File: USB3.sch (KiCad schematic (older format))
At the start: 0 parts

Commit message: Added USB SRAM sheet,Added USB3 ethernet ic
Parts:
- added C?: 100nF, Capacitor_SMD:C_0603_1608Metric_Pad1.08x0.95mm_HandSolder, symbol Device:C_Small
- added IC?: M24M02-DRMN6TP, SOIC127P600X175-8N, symbol GM_Memory_EEPROM:M24M02-DRMN6TP
- added R? (x2): 2K, Resistor_SMD:R_0603_1608Metric_Pad0.98x0.95mm_HandSolder, symbol Device:R_Small_US
- added U? (x3): CYUSB3014-BZXI, Package_BGA:BGA121C80P11X11_1000X1000X120, symbol GM_Microcontrollers:CYUSB3014-BZXI
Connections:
- net labels added: DQ[0:15], DQ[16:31], GNDD, I2C_SCL, I2C_SDA, V3P3
- wire segments 0 -> 49
- no-connect marks 0 -> 5

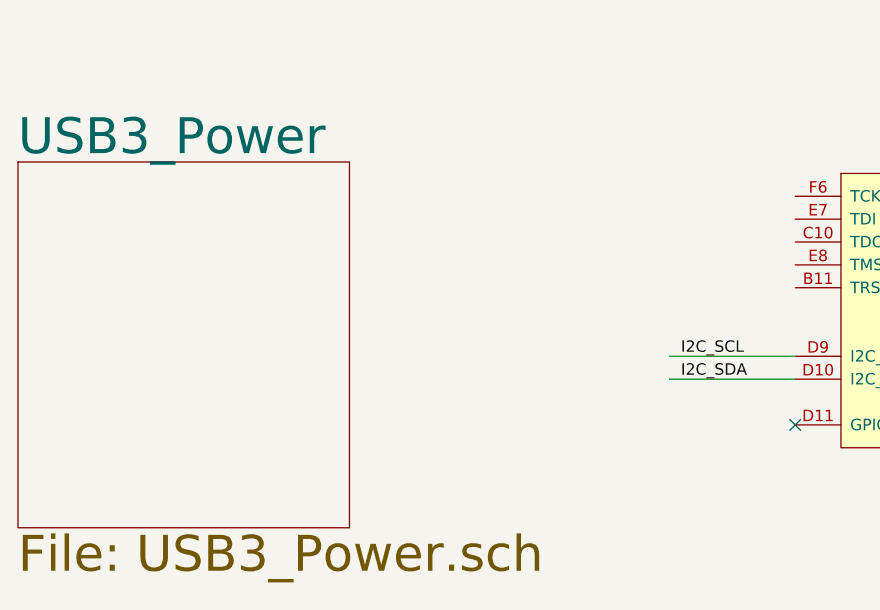
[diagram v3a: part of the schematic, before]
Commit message: Added USB3 SRAM Added 5V regulator
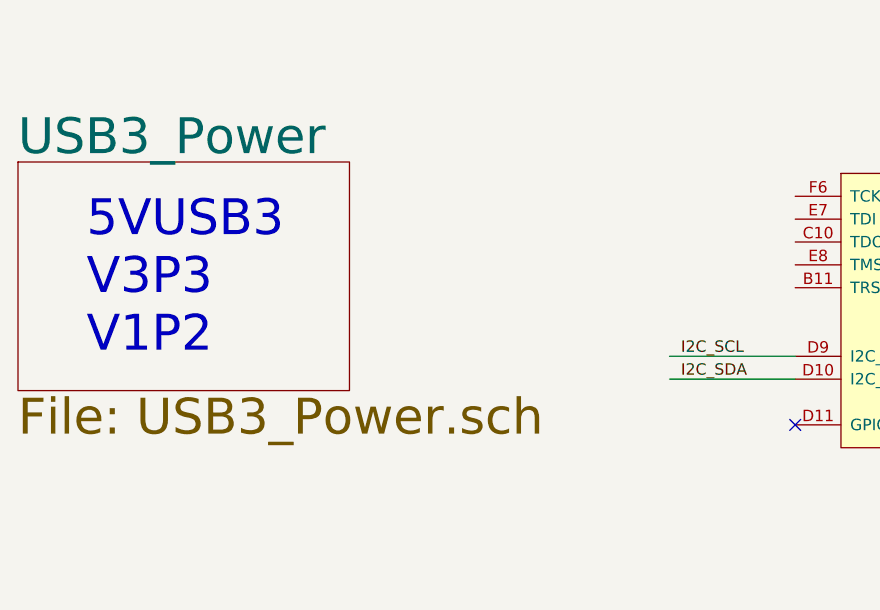
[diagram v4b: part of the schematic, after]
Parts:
- removed C?: 100nF, Capacitor_SMD:C_0603_1608Metric_Pad1.08x0.95mm_HandSolder, symbol Device:C_Small
- removed IC?: M24M02-DRMN6TP, SOIC127P600X175-8N, symbol GM_Memory_EEPROM:M24M02-DRMN6TP
- removed R?: 2K, Resistor_SMD:R_0603_1608Metric_Pad0.98x0.95mm_HandSolder, symbol Device:R_Small_US
- removed U? (x3): CYUSB3014-BZXI, Package_BGA:BGA121C80P11X11_1000X1000X120, symbol GM_Microcontrollers:CYUSB3014-BZXI
- added C?: 100nF, Capacitor_SMD:C_0603_1608Metric_Pad1.08x0.95mm_HandSolder, symbol Device:C_Small
- added IC?: M24M02-DRMN6TP, SOIC127P600X175-8N, symbol GM_Memory_EEPROM:M24M02-DRMN6TP
- added R?: 2K, Resistor_SMD:R_0603_1608Metric_Pad0.98x0.95mm_HandSolder, symbol Device:R_Small_US
- added U? (x3): CYUSB3014-BZXI, Package_BGA:BGA121C80P11X11_1000X1000X120, symbol GM_Microcontrollers:CYUSB3014-BZXI
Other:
- note added: "5VUSB3\nV3P3\nV1P2"
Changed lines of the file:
@@
 $EndDescr
 $Sheet
-S 750  5700 1450 1600
-U 60277424
+S 750  5700 1450 1000
+U 603E2782
 F0 "USB3_Power" 157
 F1 "USB3_Power.sch" 157
@@
 $Comp
 L GM_Microcontrollers:CYUSB3014-BZXI U?
-U 2 1 603A79A2
+U 2 1 603E3C7F
 P 4350 1250
 F 0 "U?" H 5000 1415 50  0000 C CNN
@@
 $Comp
 L GM_Microcontrollers:CYUSB3014-BZXI U?
-U 3 1 603A9E58
+U 3 1 603E3C80
 P 4350 5750
 F 0 "U?" H 5218 5196 50  0000 L CNN
@@
 $Comp
 L GM_Microcontrollers:CYUSB3014-BZXI U?
-U 4 1 603AE481
+U 4 1 603E2786
 P 6350 5750
 F 0 "U?" H 6928 5196 50  0000 L CNN
@@
 $Comp
 L GM_Memory_EEPROM:M24M02-DRMN6TP IC?
-U 1 1 603D536E
+U 1 1 603E2787
 P 9200 5600
 F 0 "IC?" H 9650 5765 50  0000 C CNN
@@
 $Comp
 L Device:C_Small C?
-U 1 1 603E2400
+U 1 1 603E2788
 P 8150 5800
-AR Path="/601DF0A6/603E2400" Ref="C?"  Part="1"
-AR Path="/601E7BBE/60277424/603E2400" Ref="C?"  Part="1"
-AR Path="/601E7BBE/603E2400" Ref="C?"  Part="1"
+AR Path="/601DF0A6/603E2788" Ref="C?"  Part="1"
+AR Path="/601E7BBE/60277424/603E2788" Ref="C?"  Part="1"
+AR Path="/601E7BBE/603E2788" Ref="C?"  Part="1"
 F 0 "C?" H 8242 5891 50  0000 L CNN
 F 1 "100nF" H 8242 5800 50  0000 L CNN
@@
 $Comp
 L power:GNDD #PWR?
-U 1 1 603E909D
+U 1 1 603E2789
 P 8150 5900
-AR Path="/601E7BBE/60277424/603E909D" Ref="#PWR?"  Part="1"
-AR Path="/601E7BBE/603E909D" Ref="#PWR?"  Part="1"
+AR Path="/601E7BBE/60277424/603E2789" Ref="#PWR?"  Part="1"
+AR Path="/601E7BBE/603E2789" Ref="#PWR?"  Part="1"
 F 0 "#PWR?" H 8150 5650 50  0001 C CNN
 F 1 "GNDD" H 8154 5745 50  0000 C CNN
@@
 $Comp
 L power:GNDD #PWR?
-U 1 1 603ED9AD
+U 1 1 603E278A
 P 10650 6000
-AR Path="/601E7BBE/60277424/603ED9AD" Ref="#PWR?"  Part="1"
-AR Path="/601E7BBE/603ED9AD" Ref="#PWR?"  Part="1"
+AR Path="/601E7BBE/60277424/603E278A" Ref="#PWR?"  Part="1"
+AR Path="/601E7BBE/603E278A" Ref="#PWR?"  Part="1"
 F 0 "#PWR?" H 10650 5750 50  0001 C CNN
 F 1 "GNDD" H 10654 5845 50  0000 C CNN
@@
 $Comp
 L Device:R_Small_US R?
-U 1 1 603F67A2
+U 1 1 603E278B
 P 8500 5900
 F 0 "R?" H 8568 5946 50  0000 L CNN
@@
 	8850 5700 8650 5700
 NoConn ~ 4150 6850
+Text Notes 1050 6550 0    157  ~ 0
+5VUSB3\nV3P3\nV1P2
 Wire Bus Line
 	3850 1200 3850 2950

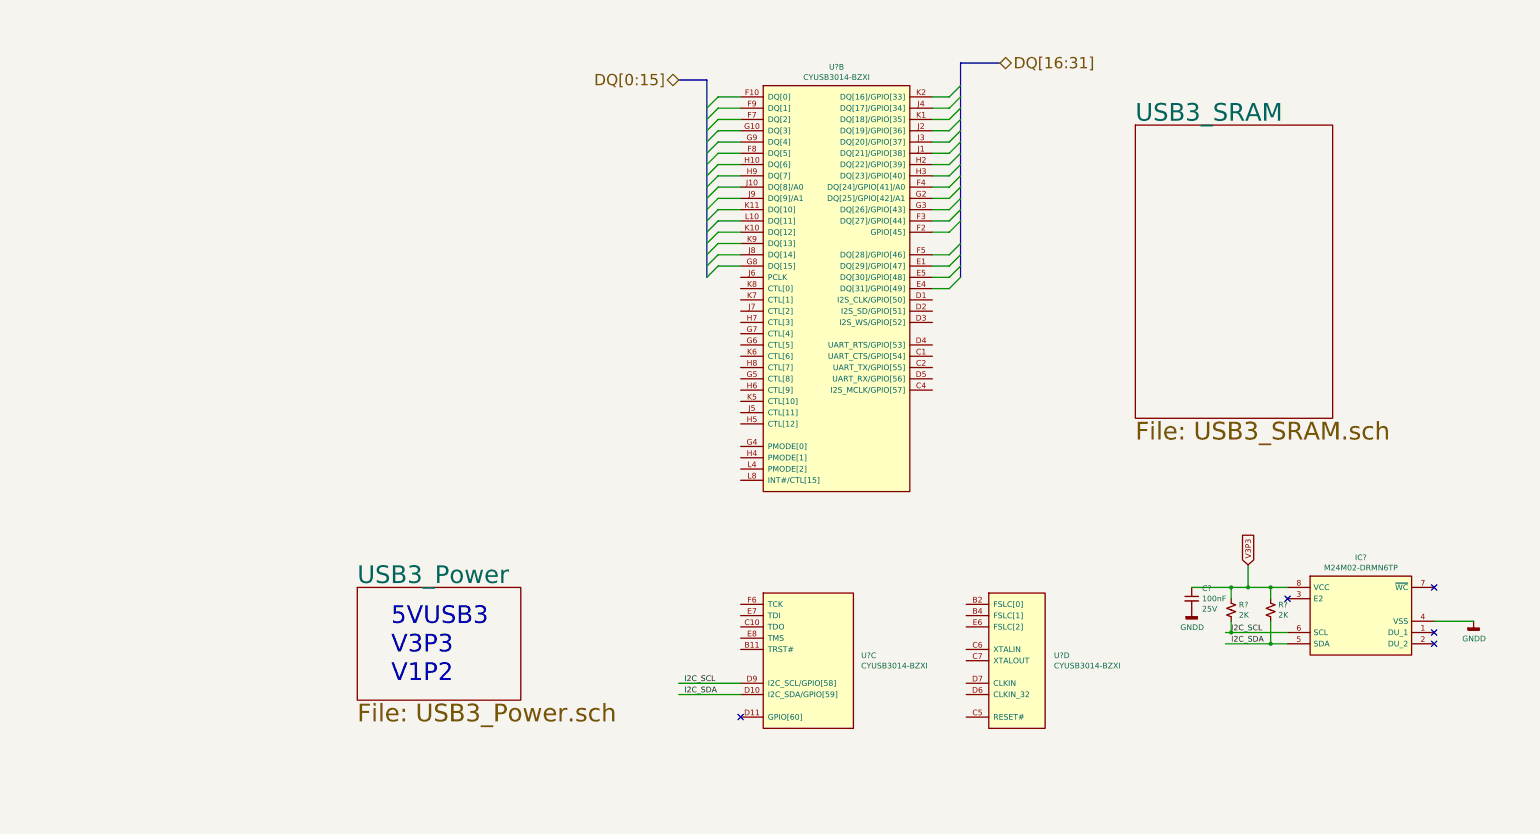
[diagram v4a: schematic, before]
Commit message: Added USB3 type B connector Added ESD protection to the same sheet
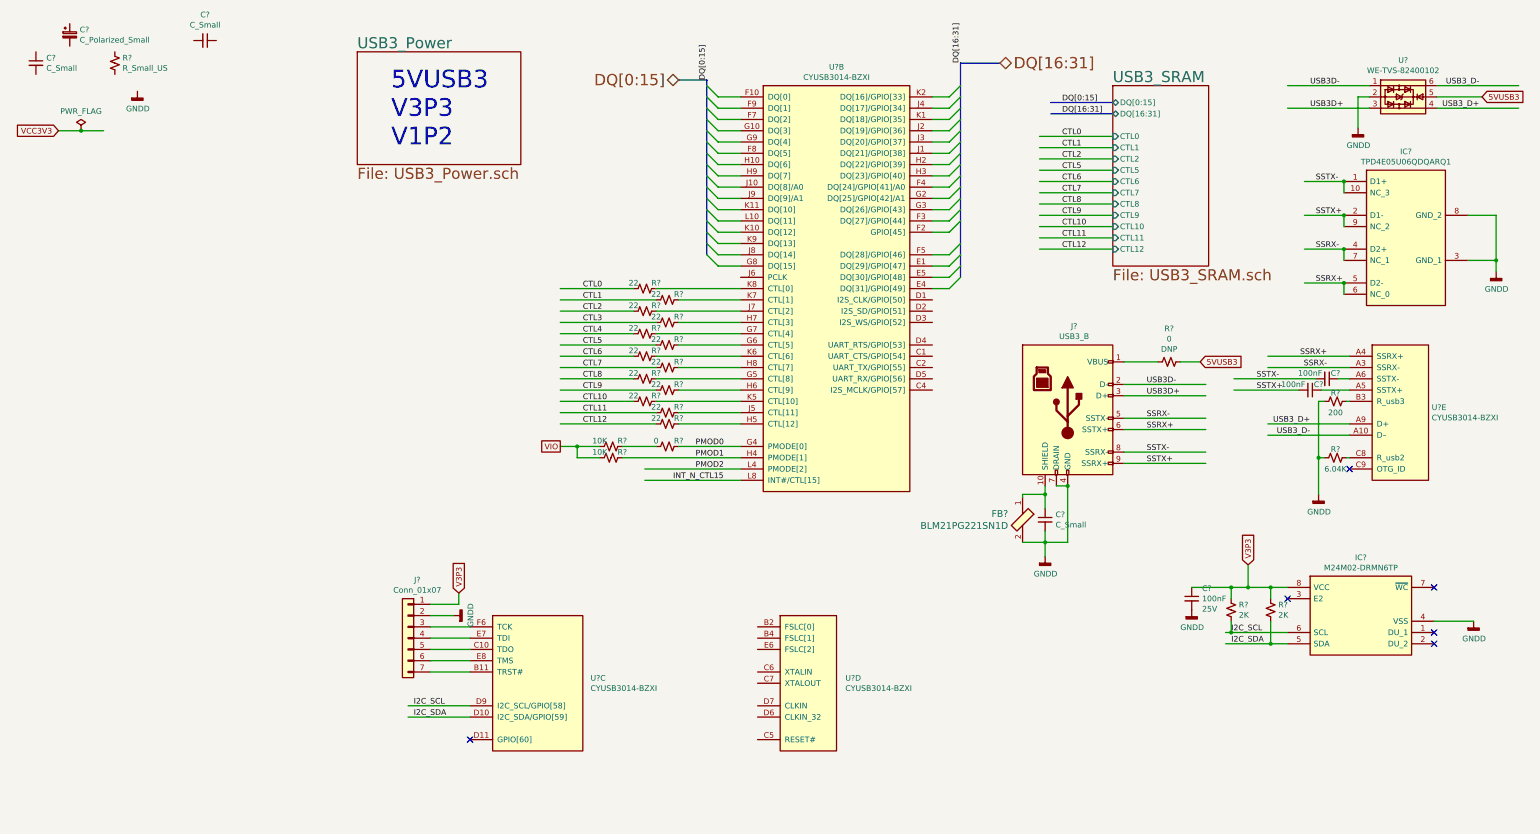
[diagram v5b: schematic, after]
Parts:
- added C? (x2): C_Small, Capacitor_SMD:C_0603_1608Metric_Pad1.08x0.95mm_HandSolder, symbol Device:C_Small
- added C?: C_Polarized_Small, Capacitor_Tantalum_SMD:CP_EIA-1608-10_AVX-L_Pad1.25x1.05mm_HandSolder, symbol Device:C_Polarized_Small
- added C?: C_Small, symbol Device:C_Small
- added C? (x2): 100nF, Capacitor_SMD:C_0402_1005Metric_Pad0.74x0.62mm_HandSolder, symbol Device:C_Small
- added FB?: BLM21PG221SN1D, digikey-footprints:0805, symbol dk_Ferrite-Beads-and-Chips:BLM21PG221SN1D
- added IC?: TPD4E05U06QDQARQ1, DQA(R-PUSON-N10), symbol GM_Protection:TPD4E05U06QDQARQ1
- added J?: Conn_01x07, symbol Connector_Generic:Conn_01x07
- added J?: USB3_B, GM_Connectors:GSB3211311WEU, symbol Connector:USB3_B
- added R?: R_Small_US, Resistor_SMD:R_0603_1608Metric_Pad0.98x0.95mm_HandSolder, symbol Device:R_Small_US
- added R? (x13): 22, Resistor_SMD:R_0603_1608Metric_Pad0.98x0.95mm_HandSolder, symbol Device:R_Small_US
- added R? (x2): 0, Resistor_SMD:R_0603_1608Metric_Pad0.98x0.95mm_HandSolder, symbol Device:R_Small_US
- added R? (x2): 10K, Resistor_SMD:R_0603_1608Metric_Pad0.98x0.95mm_HandSolder, symbol Device:R_Small_US
- added R?: 200, Resistor_SMD:R_0603_1608Metric_Pad0.98x0.95mm_HandSolder, symbol Device:R_Small_US
- added R?: 6.04K, Resistor_SMD:R_0603_1608Metric_Pad0.98x0.95mm_HandSolder, symbol Device:R_Small_US
- added U?: CYUSB3014-BZXI, Package_BGA:BGA121C80P11X11_1000X1000X120, symbol GM_Microcontrollers:CYUSB3014-BZXI
- added U?: WE-TVS-82400102, Package_TO_SOT_SMD:SOT-23-6, symbol Power_Protection:WE-TVS-82400102
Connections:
- net labels added: 5VUSB3, CTL0, CTL1, CTL10, CTL11, CTL12, CTL2, CTL3, CTL4, CTL5, CTL6, CTL7, CTL8, CTL9, INT_N_CTL15, PMOD0, PMOD1, PMOD2, SSRX+, SSRX-, SSTX+, SSTX-, USB3D+, USB3D-, USB3_D+, USB3_D-, VCC3V3, VIO
- wire segments 49 -> 156
- no-connect marks 5 -> 6
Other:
- moved on the sheet: U?C, U?D

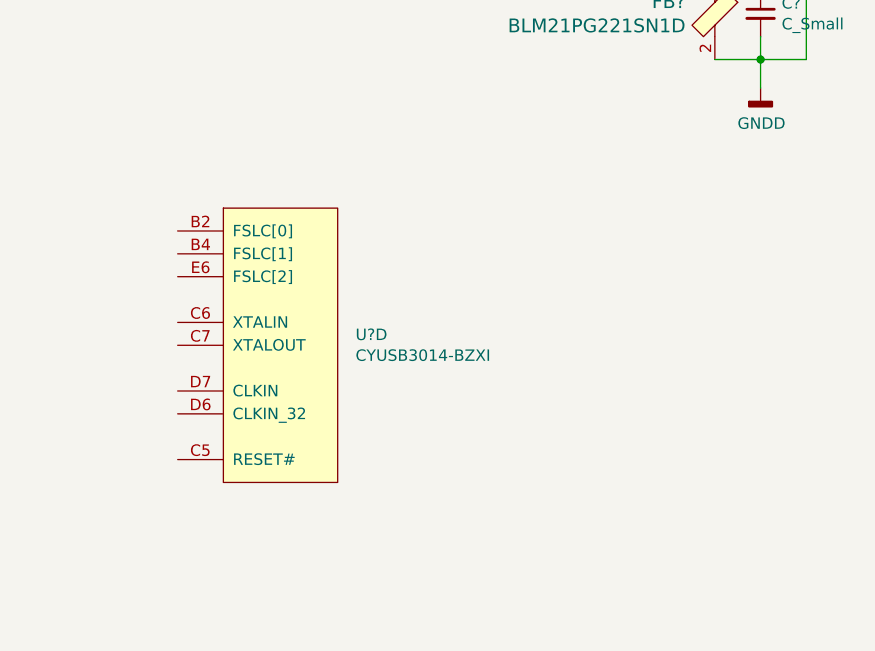
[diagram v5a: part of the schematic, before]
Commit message: Completed FPGA power sheet completed USB3 completed FPGA config
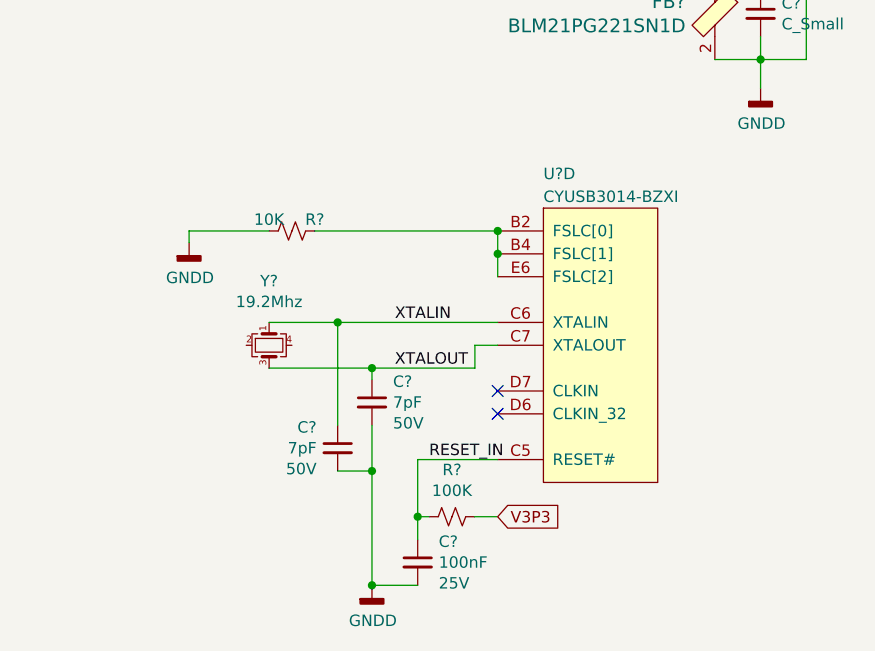
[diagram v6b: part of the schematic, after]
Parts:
- added C? (x2): 7pF, Capacitor_SMD:C_0603_1608Metric_Pad1.08x0.95mm_HandSolder, symbol Device:C_Small
- added C?: 100nF, Capacitor_SMD:C_0603_1608Metric_Pad1.08x0.95mm_HandSolder, symbol Device:C_Small
- added R?: 10K, Resistor_SMD:R_0603_1608Metric_Pad0.98x0.95mm_HandSolder, symbol Device:R_Small_US
- added R?: 100K, Resistor_SMD:R_0603_1608Metric_Pad0.98x0.95mm_HandSolder, symbol Device:R_Small_US
- added Y?: 19.2Mhz, Crystal:Crystal_SMD_Abracon_ABM10-4Pin_2.5x2.0mm, symbol Device:Crystal_GND24_Small
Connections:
- net labels added: RESET_IN, XTALIN, XTALOUT
- wire segments 156 -> 178
- no-connect marks 6 -> 8
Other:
- moved on the sheet: U?D
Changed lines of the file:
@@
 L GM_Microcontrollers:CYUSB3014-BZXI U?
 U 4 1 603E2786
-P 4500 5950
-F 0 "U?" H 5078 5396 50  0000 L CNN
-F 1 "CYUSB3014-BZXI" H 5078 5305 50  0000 L CNN
-F 2 "Package_BGA:BGA121C80P11X11_1000X1000X120" H 4800 6150 50  0001 C CNN
-F 3 "https://www.cypress.com/file/140296/download" H 4800 6150 50  0001 C CNN
-F 4 "CYUSB3014-BZXI" H 4500 5950 50  0001 C CNN "MPN"
-	4    4500 5950
+P 5900 5950
+F 0 "U?" H 5900 6100 50  0000 L CNN
+F 1 "CYUSB3014-BZXI" H 5900 6000 50  0000 L CNN
+F 2 "Package_BGA:BGA121C80P11X11_1000X1000X120" H 6200 6150 50  0001 C CNN
+F 3 "https://www.cypress.com/file/140296/download" H 6200 6150 50  0001 C CNN
+F 4 "CYUSB3014-BZXI" H 5900 5950 50  0001 C CNN "MPN"
+	4    5900 5950
 	1    0    0    -1
 $EndComp
@@
 Wire Wire Line
 	10600 2800 10850 2800
+Connection ~ 10850 2800
+Wire Wire Line
+	10850 2800 10850 2900
+$Comp
+L Device:R_Small_US R?
+U 1 1 60337DA9
+P 4800 6050
+AR Path="/601E7C5A/60337DA9" Ref="R?"  Part="1"
+AR Path="/601E7CC8/60337DA9" Ref="R?"  Part="1"
+AR Path="/601E7C92/60337DA9" Ref="R?"  Part="1"
+AR Path="/601E7C92/60257FE5/60337DA9" Ref="R?"  Part="1"
+AR Path="/601E7B38/60337DA9" Ref="R?"  Part="1"
+AR Path="/601DF0A6/60337DA9" Ref="R?"  Part="1"
+AR Path="/601E7BBE/60337DA9" Ref="R?"  Part="1"
+F 0 "R?" V 4750 6150 50  0000 C CNN
+F 1 "10K" V 4750 5950 50  0000 C CNN
+F 2 "Resistor_SMD:R_0603_1608Metric_Pad0.98x0.95mm_HandSolder" H 4800 6050 50  0001 C CNN
+F 3 "~" H 4800 6050 50  0001 C CNN
+	1    4800 6050
+	0    1    1    0
+$EndComp
+Wire Wire Line
+	5700 6050 4900 6050
+Wire Wire Line
+	5700 6250 5700 6150
+Connection ~ 5700 6050
+Connection ~ 5700 6150
+Wire Wire Line
+	5700 6150 5700 6050
+$Comp
+L power:GNDD #PWR?
+U 1 1 6034D051
+P 4350 6100
+AR Path="/601E7BBE/60277424/6034D051" Ref="#PWR?"  Part="1"
+AR Path="/601E7BBE/6034D051" Ref="#PWR?"  Part="1"
+F 0 "#PWR?" H 4350 5850 50  0001 C CNN
+F 1 "GNDD" H 4354 5945 50  0000 C CNN
+F 2 "" H 4350 6100 50  0001 C CNN
+F 3 "" H 4350 6100 50  0001 C CNN
+	1    4350 6100
+	1    0    0    -1
+$EndComp
+Wire Wire Line
+	4350 6100 4350 6050
+Wire Wire Line
+	4350 6050 4700 6050
+$Comp
+L Device:Crystal_GND24_Small Y?
+U 1 1 6035B9D1
+P 4700 6550
+F 0 "Y?" V 4419 6550 50  0000 C CNN
+F 1 "19.2Mhz" V 4510 6550 50  0000 C CNN
+F 2 "Crystal:Crystal_SMD_Abracon_ABM10-4Pin_2.5x2.0mm" H 4700 6550 50  0001 C CNN
+F 3 "~" H 4700 6550 50  0001 C CNN
+F 4 "NX2520SG-19.2M-STD-CTX-1" V 4700 6550 50  0001 C CNN "MPN"
+	1    4700 6550
+	0    1    1    0
+$EndComp
+$Comp
+L Device:C_Small C?
+U 1 1 6035CB90
+P 5150 6800
+AR Path="/601E7C5A/6035CB90" Ref="C?"  Part="1"
+AR Path="/601E7CC8/6035CB90" Ref="C?"  Part="1"
+AR Path="/601E7C92/6035CB90" Ref="C?"  Part="1"
+AR Path="/601E7C92/60257FE5/6035CB90" Ref="C?"  Part="1"
+AR Path="/601E7B38/6035CB90" Ref="C?"  Part="1"
+AR Path="/601DF0A6/6035CB90" Ref="C?"  Part="1"
+AR Path="/601E7BBE/6035CB90" Ref="C?"  Part="1"
+F 0 "C?" H 5242 6891 50  0000 L CNN
+F 1 "7pF" H 5242 6800 50  0000 L CNN
+F 2 "Capacitor_SMD:C_0603_1608Metric_Pad1.08x0.95mm_HandSolder" H 5150 6800 50  0001 C CNN
+F 3 "~" H 5150 6800 50  0001 C CNN
+F 4 "50V" H 5242 6709 50  0000 L CNN "Voltage"
+	1    5150 6800
+	1    0    0    -1
+$EndComp
+Wire Wire Line
+	4700 6450 5000 6450
+Wire Wire Line
+	5700 6550 5600 6550
+Wire Wire Line
+	5600 6550 5600 6650
+Wire Wire Line
+	5600 6650 5150 6650
+Wire Wire Line
+	5000 6900 5000 6450
+Connection ~ 5000 6450
+Wire Wire Line
+	5000 6450 5700 6450
+Wire Wire Line
+	5150 6700 5150 6650
+Connection ~ 5150 6650
+Wire Wire Line
+	5150 6650 4700 6650
+$Comp
+L power:GNDD #PWR?
+U 1 1 6038C3EE
+P 5150 7600
+AR Path="/601E7BBE/60277424/6038C3EE" Ref="#PWR?"  Part="1"
+AR Path="/601E7BBE/6038C3EE" Ref="#PWR?"  Part="1"
+F 0 "#PWR?" H 5150 7350 50  0001 C CNN
+F 1 "GNDD" H 5154 7445 50  0000 C CNN
+F 2 "" H 5150 7600 50  0001 C CNN
+F 3 "" H 5150 7600 50  0001 C CNN
+	1    5150 7600
+	1    0    0    -1
+$EndComp
+Wire Wire Line
+	5150 7600 5150 7100
+Connection ~ 5150 7100
+Wire Wire Line
+	5150 7100 5150 6900
+Wire Wire Line
+	5000 7100 5150 7100
+Text Label 5250 6450 0    50   ~ 0
+XTALIN
+Text Label 5250 6650 0    50   ~ 0
+XTALOUT
+$Comp
+L Device:C_Small C?
+U 1 1 603CE099
+P 5000 7000
+AR Path="/601E7C5A/603CE099" Ref="C?"  Part="1"
+AR Path="/601E7CC8/603CE099" Ref="C?"  Part="1"
+AR Path="/601E7C92/603CE099" Ref="C?"  Part="1"
+AR Path="/601E7C92/60257FE5/603CE099" Ref="C?"  Part="1"
+AR Path="/601E7B38/603CE099" Ref="C?"  Part="1"
+AR Path="/601DF0A6/603CE099" Ref="C?"  Part="1"
+AR Path="/601E7BBE/603CE099" Ref="C?"  Part="1"
+F 0 "C?" H 4908 7091 50  0000 R CNN
+F 1 "7pF" H 4908 7000 50  0000 R CNN
+F 2 "Capacitor_SMD:C_0603_1608Metric_Pad1.08x0.95mm_HandSolder" H 5000 7000 50  0001 C CNN
+F 3 "~" H 5000 7000 50  0001 C CNN
+F 4 "50V" H 4908 6909 50  0000 R CNN "Voltage"
+	1    5000 7000
+	1    0    0    -1
+$EndComp
+NoConn ~ 5700 6750
+NoConn ~ 5700 6850
+Text Label 5400 7050 0    50   ~ 0
+RESET_IN
+Wire Wire Line
+	5350 7050 5700 7050
+$Comp
+L Device:R_Small_US R?
+U 1 1 60408CBC
+P 5500 7300
+AR Path="/601E7C5A/60408CBC" Ref="R?"  Part="1"
+AR Path="/601E7CC8/60408CBC" Ref="R?"  Part="1"
+AR Path="/601E7C92/60408CBC" Ref="R?"  Part="1"
+AR Path="/601E7C92/60257FE5/60408CBC" Ref="R?"  Part="1"
+AR Path="/601E7B38/60408CBC" Ref="R?"  Part="1"
+AR Path="/601DF0A6/60408CBC" Ref="R?"  Part="1"
+AR Path="/601E7BBE/60408CBC" Ref="R?"  Part="1"
+F 0 "R?" V 5295 7300 50  0000 C CNN
+F 1 "100K" V 5386 7300 50  0000 C CNN
+F 2 "Resistor_SMD:R_0603_1608Metric_Pad0.98x0.95mm_HandSolder" H 5500 7300 50  0001 C CNN
+F 3 "~" H 5500 7300 50  0001 C CNN
+	1    5500 7300
+	0    1    1    0
+$EndComp
+Text GLabel 5700 7300 2    50   Input ~ 0
+V3P3
+$Comp
+L Device:C_Small C?
+U 1 1 6040A2B1
+P 5350 7500
+AR Path="/601E7C5A/6040A2B1" Ref="C?"  Part="1"
+AR Path="/601E7CC8/6040A2B1" Ref="C?"  Part="1"
+AR Path="/601E7C92/6040A2B1" Ref="C?"  Part="1"
+AR Path="/601E7C92/60257FE5/6040A2B1" Ref="C?"  Part="1"
+AR Path="/601E7B38/6040A2B1" Ref="C?"  Part="1"
+AR Path="/601DF0A6/6040A2B1" Ref="C?"  Part="1"
+AR Path="/601E7BBE/6040A2B1" Ref="C?"  Part="1"
+F 0 "C?" H 5442 7591 50  0000 L CNN
+F 1 "100nF" H 5442 7500 50  0000 L CNN
+F 2 "Capacitor_SMD:C_0603_1608Metric_Pad1.08x0.95mm_HandSolder" H 5350 7500 50  0001 C CNN
+F 3 "~" H 5350 7500 50  0001 C CNN
+F 4 "25V" H 5442 7409 50  0000 L CNN "Voltage"
+	1    5350 7500
+	1    0    0    -1
+$EndComp
+Wire Wire Line
+	5350 7600 5150 7600
+Connection ~ 5150 7600
+Wire Wire Line
+	5350 7400 5350 7300
+Wire Wire Line
+	5400 7300 5350 7300
+Connection ~ 5350 7300
+Wire Wire Line
+	5350 7300 5350 7050
+Wire Wire Line
+	5600 7300 5700 7300
 Wire Bus Line
 	3850 1200 3850 2750
 Wire Bus Line
 	6100 1050 6100 2950
-Connection ~ 10850 2800
-Wire Wire Line
-	10850 2800 10850 2900
 $EndSCHEMATC
